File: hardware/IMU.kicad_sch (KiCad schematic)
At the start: 21 parts, among them J1 USB_B_Micro, J2 Conn_01x07, J4 Conn_ARM_SWD_TagConnect_TC2030, U1 STM32F401RCTx, U2 HT75xx-1-SOT89, U3 ISM330DLCTR, U4 STM32F401RCT6TR

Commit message: first draft schematic
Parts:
- removed J2: Conn_01x07, symbol Connector_Generic:Conn_01x07
- removed J4: Conn_ARM_SWD_TagConnect_TC2030, Connector:Tag-Connect_TC2030-IDC-FP_2x03_P1.27mm_Vertical, symbol Connector:Conn_ARM_SWD_TagConnect_TC2030
- removed U1: STM32F401RCTx, Package_QFP:LQFP-64_10x10mm_P0.5mm, symbol MCU_ST_STM32F4:STM32F401RCTx
- added C12, C13: 100nF, symbol Device:C
- added J2: Conn_01x10_MountingPin, symbol Connector_Generic_MountingPin:Conn_01x10_MountingPin
- added J3, J5: Conn_01x04_MountingPin, symbol Connector_Generic_MountingPin:Conn_01x04_MountingPin
- added J7: Conn_02x03_Counter_Clockwise, symbol Connector_Generic:Conn_02x03_Counter_Clockwise
- added R2: 10k?, symbol Device:R
- C7: value 4.7μF -> 100nF
- C8: value 100nF -> 4.7μF
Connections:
- net GND: now also U3.1 (SDO/SAO), U3.2 (SDX), U3.3 (SCX), U3.6 (GND), U3.7 (GND__1), U4.12 (VSSA/VREF-), U4.18 (VSS), U4.31 (VSS__1), U4.47 (VSS__2), U4.63 (VSS__3), C12.2, C13.2, J2.6 (Pin_6), J3.4 (Pin_4), J5.4 (Pin_4), J7.4 (Pin_4), R2.1
- net PWR: now also C7.1, C9.1, U3.12 (CS), U3.5 (VDDIO), U3.8 (VDD), U4.13 (VDDA/VREF+), C12.1, C13.1, J2.5 (Pin_5), J3.3 (Pin_3), J5.1 (Pin_1), J7.1 (Pin_1)
- net RST: now reaches C1.1
- net RST: now also U4.7 (~{RST}), J7.6 (Pin_6)
- net at C8.1: now also U4.30 (VCAP_1); no longer C9.1
- net TX: now reaches U4.16 (PA2)
- net TX: now also J5.2 (Pin_2)
- net RX: now reaches U4.17 (PA3)
- net RX: now also J5.3 (Pin_3)
- net INT1: now reaches U4.27 (PB1)
- net INT1: now also U3.4 (INT1)
- net INT2: now reaches U4.28 (PB2)
- net INT2: now also U3.9 (INT2)
- net at U4.33 (PB12): now also J2.1 (Pin_1)
- net at U4.34 (PB13): now also J2.2 (Pin_2)
- net at U4.35 (PB14): now also J2.3 (Pin_3)
- net at U4.36 (PB15): now also J2.4 (Pin_4)
- net at U4.37 (PC6): now also J2.7 (Pin_7)
- net at U4.38 (PC7): now also J2.8 (Pin_8)
- net at U4.39 (PC8): now also J2.9 (Pin_9)
- net at U4.40 (PC9): now also J2.10 (Pin_10)
- net SWDIO: now reaches U4.46 (PA13/JTMS-SWDIO)
- net SWDIO: now also J7.2 (Pin_2)
- net SWCLK: now reaches U4.49 (PA14/JTCK-SWCLK)
- net SWCLK: now also J7.3 (Pin_3)
- net SWO: now reaches U4.55 (PB3/JTDO-SWO)
- net SWO: now also J7.5 (Pin_5)
- net SCL: now reaches U4.58 (PB6)
- net SCL: now also U3.13 (SCL), J3.1 (Pin_1)
- net SDA: now reaches U4.59 (PB7)
- net SDA: now also U3.14 (SDA), J3.2 (Pin_2)
- net at U4.60 (BOOT0): now also R2.2
- no-connect marks 4 -> 39
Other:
- note added: "IMU"
- note added: "IMU Sensor with STM32"
- note added: "MCU"
- note added: "Nithya Sudharshan"
- note added: "SDA"
- note added: "SWD Headers"
- note added: "Test Headers for IMU"
- note added: "UART Headers"
- note removed: "SWCLK"
- note removed: "SWDIO"
- moved on the sheet: C1, C10, C11, C2, C3, C4, C5, C6, C9, D1, D2, R1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

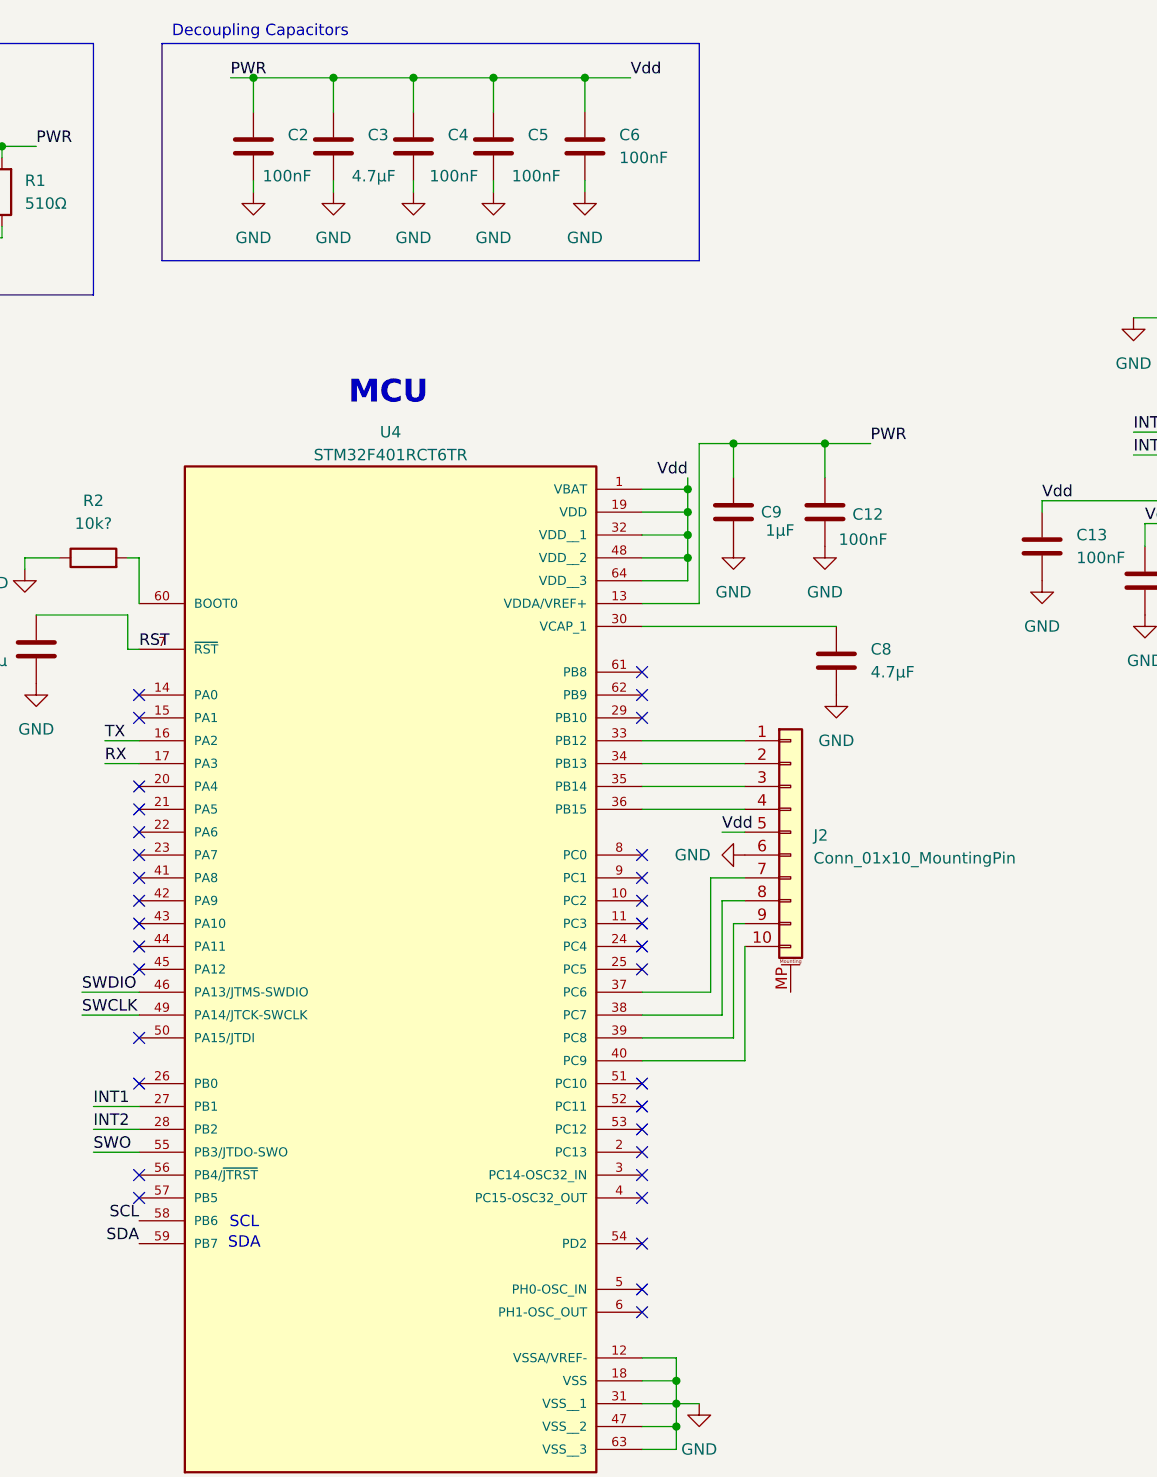
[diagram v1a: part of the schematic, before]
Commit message: added clock and other stuff
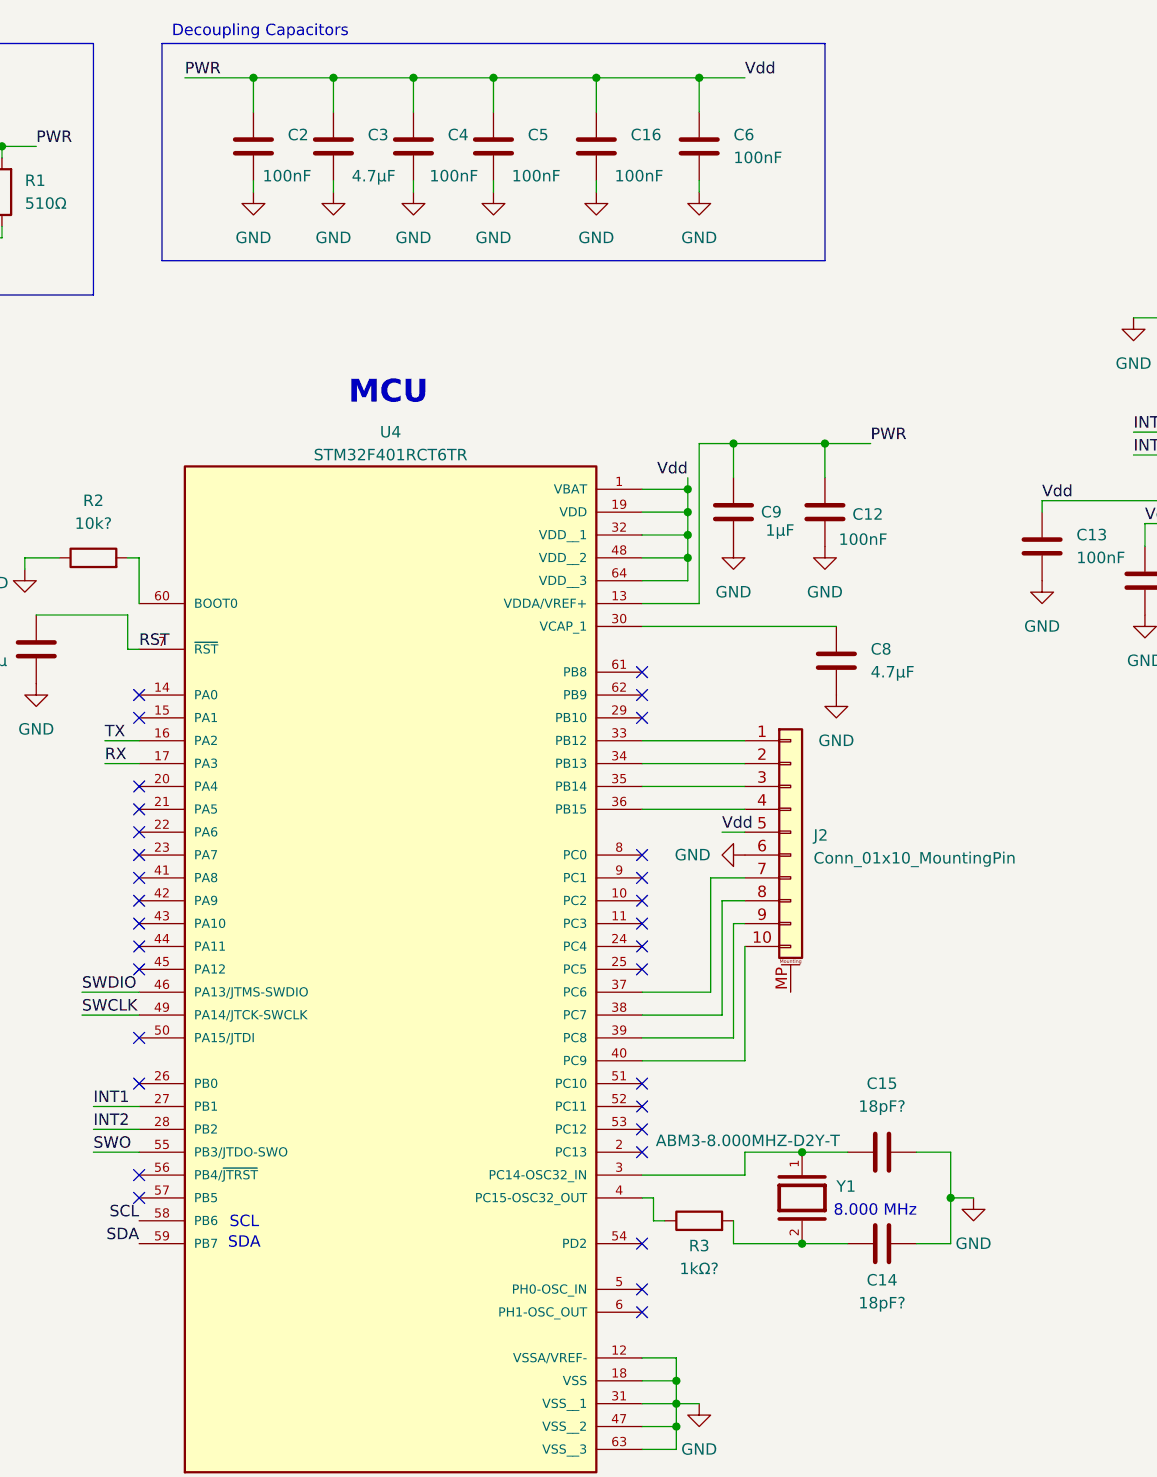
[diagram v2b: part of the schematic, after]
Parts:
- added C14, C15: 18pF?, symbol Device:C
- added C16: 100nF, symbol Device:C
- added R3: 1kΩ?, symbol Device:R
- added Y1: ABM3-8.000MHZ-D2Y-T, My_library:XTAL_ABM3-8.000MHZ-D2Y-T, symbol My_library:ABM3-8.000MHZ-D2Y-T
- J1: footprint (none) -> Connector_USB:USB_Micro-B_GCT_USB3076-30-A
- U4: footprint STM32F401RCT6TR:QFP50P1200X1200X160-64N -> My_library:STM32F4QFP50P1200X1200X160-64N
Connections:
- net GND: now also C14.1, C15.2, C16.2
- net PWR: now also C16.1
- net at U4.3 (PC14-OSC32_IN): now also C15.1, Y1.1
- net at U4.4 (PC15-OSC32_OUT): now also R3.1
- new net: C14.2, R3.2, Y1.2
- no-connect marks 39 -> 37
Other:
- note added: "8.000 MHz"
- moved on the sheet: C6

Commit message: fixed crystal and misc
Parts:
- removed J2: Conn_01x10_MountingPin, symbol Connector_Generic_MountingPin:Conn_01x10_MountingPin
- removed J3, J5: Conn_01x04_MountingPin, symbol Connector_Generic_MountingPin:Conn_01x04_MountingPin
- removed J7: Conn_02x03_Counter_Clockwise, symbol Connector_Generic:Conn_02x03_Counter_Clockwise
- removed Y1: ABM3-8.000MHZ-D2Y-T, My_library:XTAL_ABM3-8.000MHZ-D2Y-T, symbol My_library:ABM3-8.000MHZ-D2Y-T
- added J2: Conn_01x09, symbol Connector_Generic:Conn_01x09
- added J4: Conn_01x10, symbol Connector_Generic:Conn_01x10
- added J6, J8: Conn_01x04, symbol Connector_Generic:Conn_01x04
- added J9: Conn_01x06, symbol Connector_Generic:Conn_01x06
- added SW1: SW_Push, symbol Switch:SW_Push
- added Y2: WE-XTAL_CFPX-104, My_library:WE-XTAL_CFPX-104, symbol My_library:WE-XTAL_CFPX-104
- C1: value 0.1μ -> 100nF
- C14, C15: value 18pF? -> 16pF
- R2: value 10k? -> 10kΩ
- R3: value 1kΩ? -> 1.2kΩ
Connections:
- net GND: now also D2.1 (K), J1.6 (Shield), J4.6 (Pin_6), J6.4 (Pin_4), J8.4 (Pin_4), J9.6 (Pin_6), Y2.2, Y2.4; no longer R1.1
- net PWR: now also D2.2 (A), R1.1, J4.5 (Pin_5), J6.1 (Pin_1), J8.3 (Pin_3), J9.1 (Pin_1); no longer D2.1 (K), R1.2
- net RST: now also J9.5 (Pin_5), SW1.2; no longer C1.1
- net RX: now also J6.3 (Pin_3)
- net SCL: now also J8.1 (Pin_1)
- net SDA: now also J8.2 (Pin_2)
- net SWCLK: now also J9.4 (Pin_4)
- net SWDIO: now also J9.3 (Pin_3)
- net SWO: now also J9.2 (Pin_2)
- net TX: now also J6.2 (Pin_2)
- net at R3.1: now also U4.6 (PH1-OSC_OUT); no longer U4.4 (PC15-OSC32_OUT)
- net at C14.2, R3.2: now also Y2.1
- net at C11.1, U2.3 (VOUT): now also R1.2; no longer D2.2 (A)
- net at U4.33 (PB12): now also J4.1 (Pin_1)
- net at U4.40 (PC9): now also J4.10 (Pin_10)
- net at U4.34 (PB13): now also J4.2 (Pin_2)
- net at U4.35 (PB14): now also J4.3 (Pin_3)
- net at U4.36 (PB15): now also J4.4 (Pin_4)
- net at U4.37 (PC6): now also J4.7 (Pin_7)
- net at U4.38 (PC7): now also J4.8 (Pin_8)
- net at U4.39 (PC8): now also J4.9 (Pin_9)
- net at C15.1: now also U4.5 (PH0-OSC_IN), Y2.3; no longer U4.3 (PC14-OSC32_IN)
- net at U4.20 (PA4): now also J2.9 (Pin_9)
- net at U4.21 (PA5): now also J2.8 (Pin_8)
- net at U4.22 (PA6): now also J2.7 (Pin_7)
- net at U4.23 (PA7): now also J2.6 (Pin_6)
- net at U4.41 (PA8): now also J2.5 (Pin_5)
- net at U4.42 (PA9): now also J2.4 (Pin_4)
- net at U4.43 (PA10): now also J2.3 (Pin_3)
- net at U4.44 (PA11): now also J2.2 (Pin_2)
- net at U4.45 (PA12): now also J2.1 (Pin_1)
- new net: C1.1, SW1.1
- no-connect marks 37 -> 27
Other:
- moved on the sheet: C1, C12, C13, C14, C15, C7, C8, C9, D2, J1, R1, R2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

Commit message: more changes
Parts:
- added H1, H2, H3, H4: MountingHole, symbol Mechanical:MountingHole
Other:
- note added: "Mounting Holes"

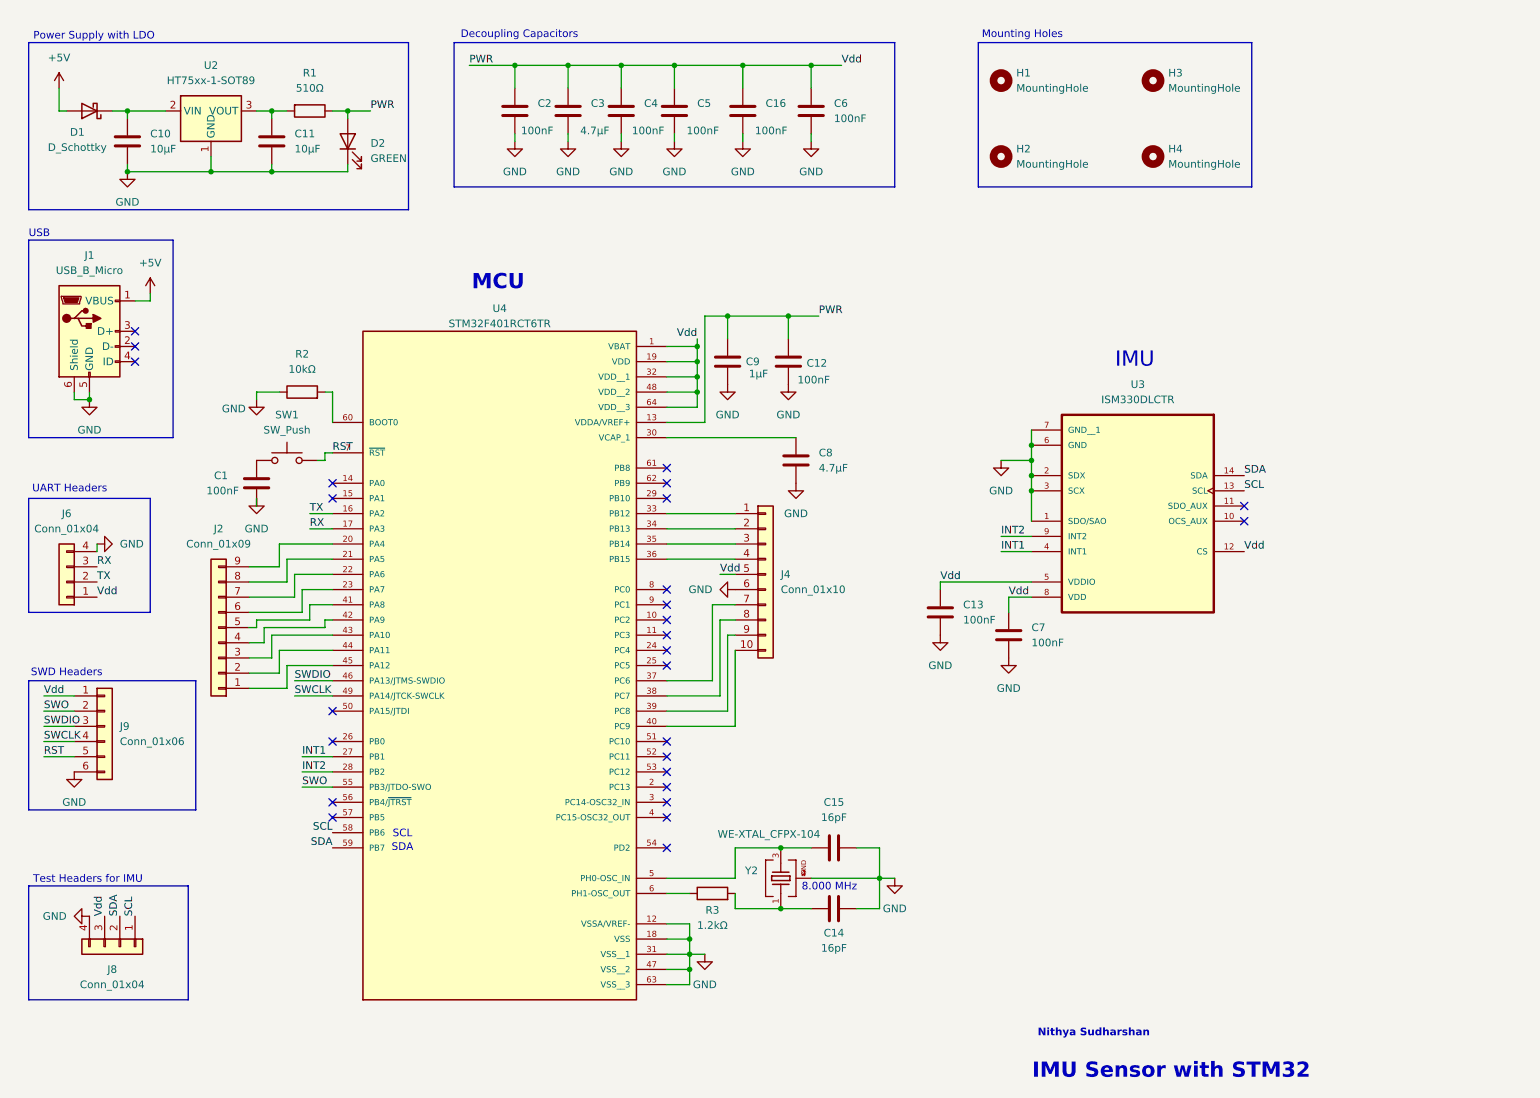
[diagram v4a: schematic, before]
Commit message: added footprints
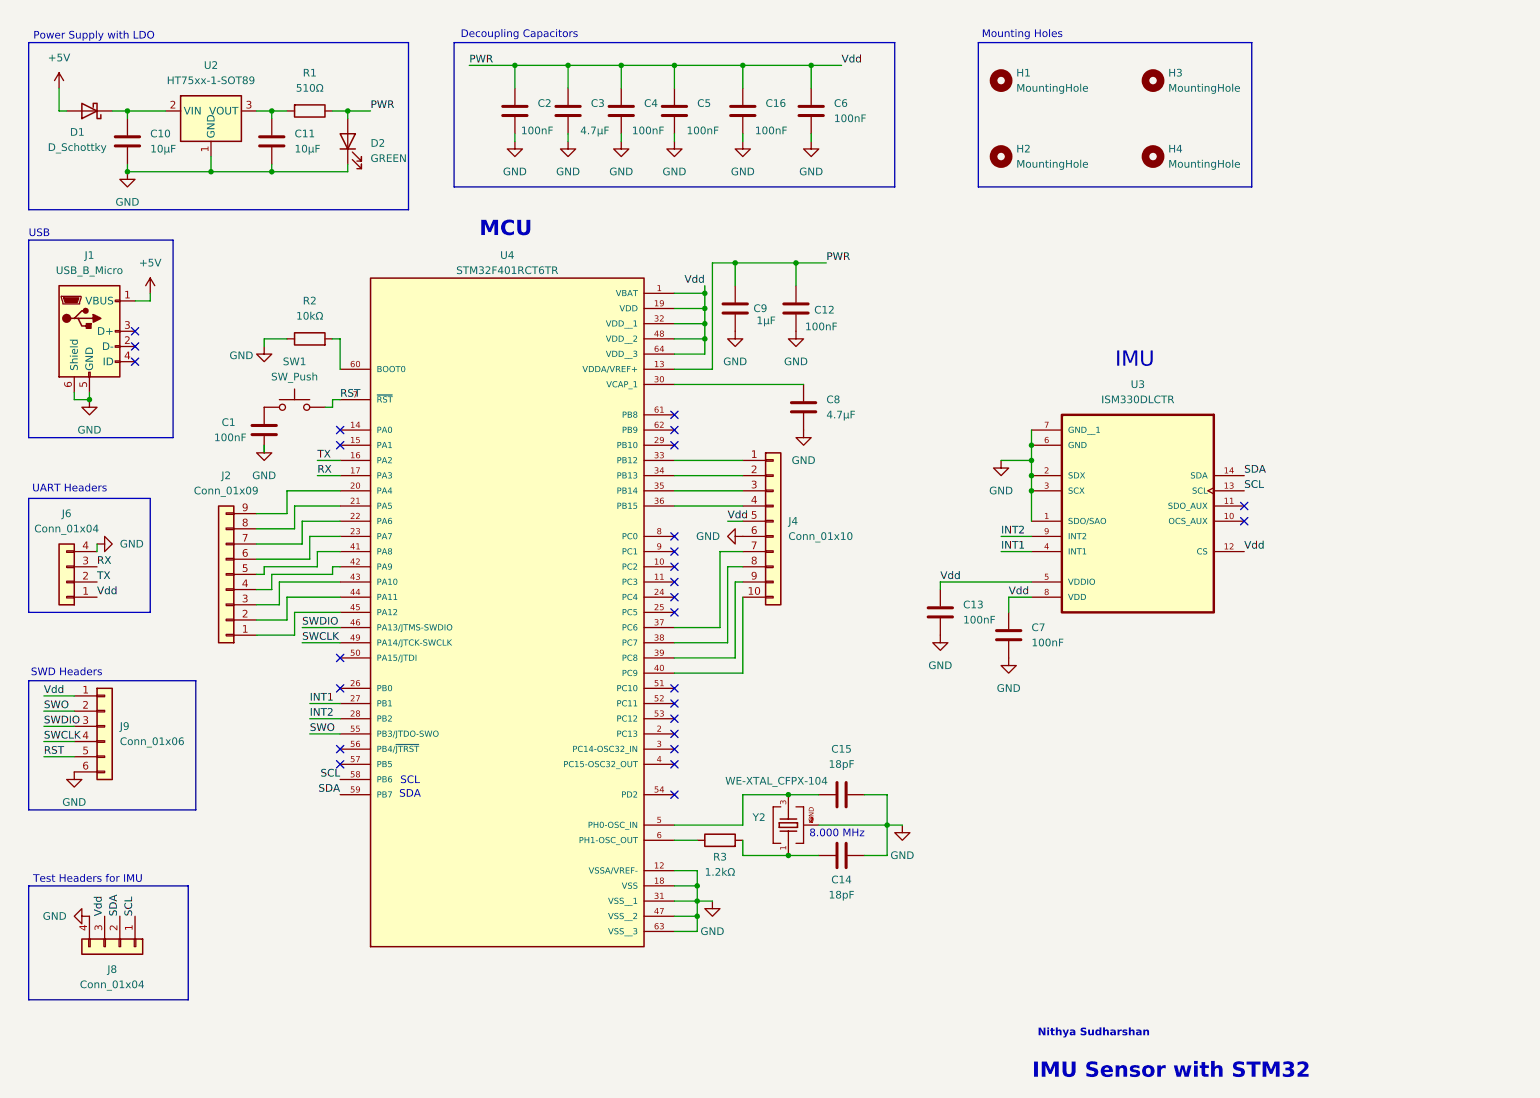
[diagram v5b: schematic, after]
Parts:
- C1: footprint Capacitor_SMD:C_0201_0603Metric -> Capacitor_SMD:C_0805_2012Metric
- C10, C11, C12, C13, C16, C2, C3, C4, C5, C6, C7, C8, C9: footprint (none) -> Capacitor_SMD:C_0805_2012Metric
- C14, C15: value 16pF -> 18pF; footprint (none) -> Capacitor_SMD:C_0805_2012Metric
- D1: footprint (none) -> Diode_SMD:D_3220_8050Metric
- D2: footprint (none) -> LED_SMD:LED_0805_2012Metric
- H1, H2, H3, H4: footprint (none) -> MountingHole:MountingHole_2.7mm_M2.5_Pad
- J2: footprint (none) -> Connector_PinHeader_2.54mm:PinHeader_1x09_P2.54mm_Vertical
- J4: footprint (none) -> Connector_PinHeader_2.54mm:PinHeader_1x10_P2.54mm_Vertical
- J6, J8: footprint (none) -> Connector_PinHeader_2.54mm:PinHeader_1x04_P2.54mm_Vertical
- J9: footprint (none) -> Connector_PinHeader_2.54mm:PinHeader_1x06_P2.54mm_Vertical
- R1, R2, R3: footprint (none) -> Resistor_SMD:R_0805_2012Metric
- SW1: footprint (none) -> Button_Switch_SMD:SW_SPST_PTS647_Sx38
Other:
- moved on the sheet: C1, C12, C14, C15, C8, C9, J2, J4, R2, R3, SW1, U4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

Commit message: (mostly) fixed ERC
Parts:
- removed J1: USB_B_Micro, Connector_USB:USB_Micro-B_GCT_USB3076-30-A, symbol Connector:USB_B_Micro
- added J3: USB_B_Micro, Connector_USB:USB_Micro-B_GCT_USB3076-30-A, symbol My_library:USB_B_Micro
- added R4: 10k?, Resistor_SMD:R_0805_2012Metric, symbol Device:R
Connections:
- net +5V: now also J3.1 (VBUS)
- net GND: now also J3.5 (GND), J3.6 (Shield)
- net at C1.1, SW1.1: now also R4.1
- net +3V3: now reaches C11.1, R1.2, U2.3 (VOUT)
- net +3V3: now also C12.1, C13.1, C16.1, C2.1, C3.1, C4.1, C5.1, C6.1, C7.1, C9.1, J4.5 (Pin_5), J6.1 (Pin_1), J8.3 (Pin_3), J9.1 (Pin_1), U3.12 (CS), U3.5 (VDDIO), U3.8 (VDD), U4.1 (VBAT), U4.13 (VDDA/VREF+), U4.19 (VDD), U4.32 (VDD__1), U4.48 (VDD__2), U4.64 (VDD__3), R4.2
- removed net PWR: C12.1, C13.1, C16.1, C2.1, C3.1, C4.1, C5.1, C6.1, C7.1, C9.1, D2.2 (A), J4.5 (Pin_5), J6.1 (Pin_1), J8.3 (Pin_3), J9.1 (Pin_1), R1.1, U3.12 (CS), U3.5 (VDDIO), U3.8 (VDD), U4.1 (VBAT), U4.13 (VDDA/VREF+), U4.19 (VDD), U4.32 (VDD__1), U4.48 (VDD__2), U4.64 (VDD__3)
- new net: D2.2 (A), R1.1
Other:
- moved on the sheet: D2, R1, R2
